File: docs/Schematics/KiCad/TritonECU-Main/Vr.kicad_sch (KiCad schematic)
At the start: 56 parts, among them J301 VR spare, U301 MAX9926UAEE+T, U302 MAX9926UAEE+T, U303 MAX9926UAEE+T

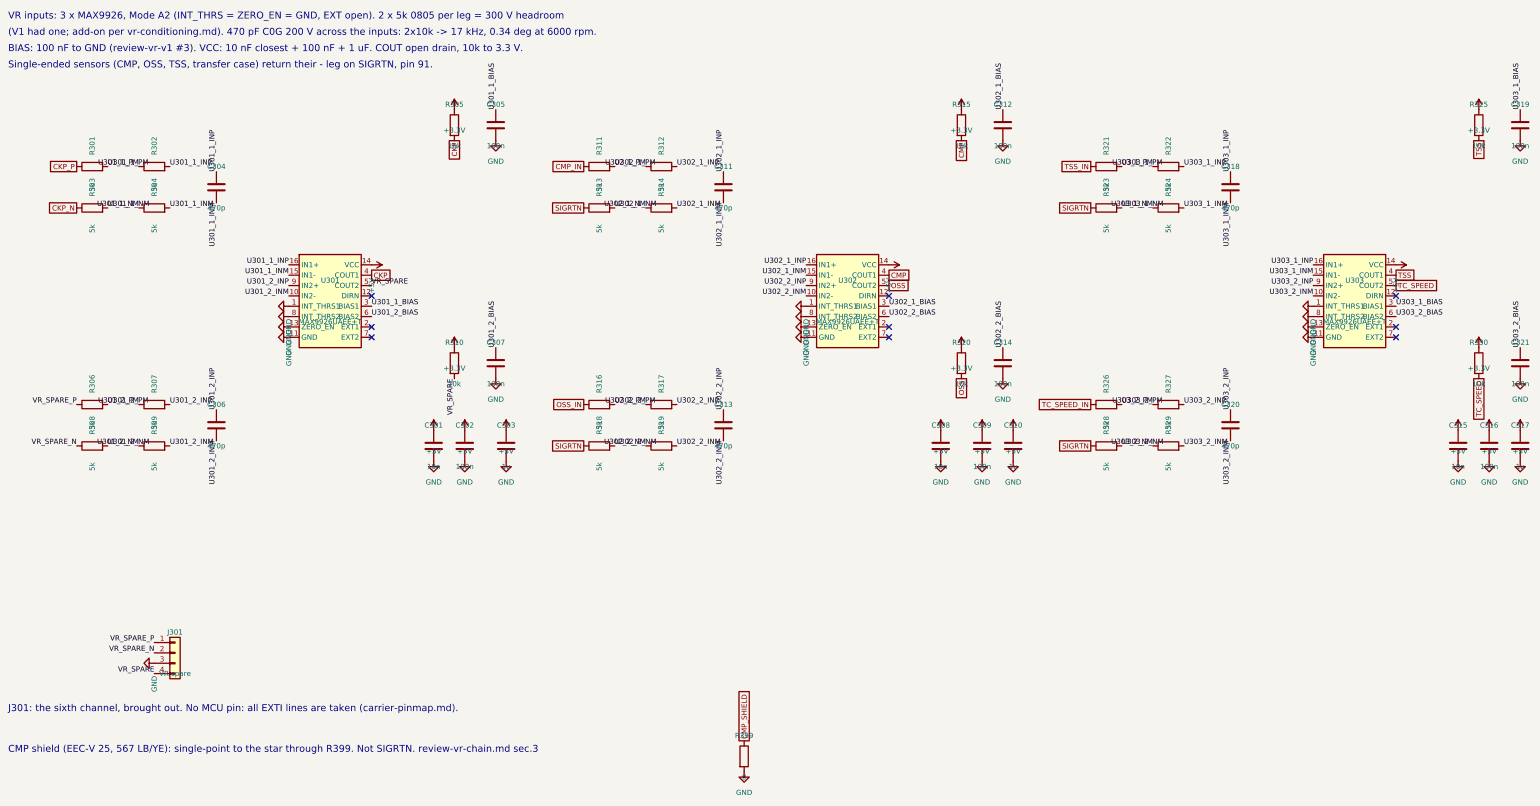
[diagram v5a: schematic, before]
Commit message: Carrier: Inputs sheet and switched rails for sleep
Inputs: one network per switch input - 4.7k pull-up to VPWR (ground-
switched only; VPWR so a TR bit closed in Park draws nothing parked),
SMF24A, 33k/15k, 10n, BAT54J to 3.3 V. TR1/2/4 and 4X4L ground-switched,
TR3A/BRAKE/ACP/TCS 12 V high-side. 4X4L mapped to EEC-V pin 14
(findings sec.14). IGN_WAKE from VPWR into PC13/WKUP4. TACH/SPEED bench
header, BOOT0 DFU solder jumper.

Switched rails: +5V and +3.3V stay up parked, so two TPS22917 load
switches on SW_RAIL_EN (PG12, 100k down) make +5V_SW / +3.3V_SW for the
running-only loads: 74HCT541 x3 and OE pull-ups, MAX9926 x3 and COUT
pull-ups, ADS8588H, OPA2376 x2, O2 bias, knock block, 74HC4051, TPS2H160B
FAULT pull-up, TFT pull-up. MCU, watchdog, CAN, SCP RX, clamps stay on.

gen_carrier_pcb.py: packer steps around existing parts, fills several
rects in turn, parks overflow below earlier parked parts.

Co-Authored-By: Claude Opus 5.5 <noreply@anthropic.com>
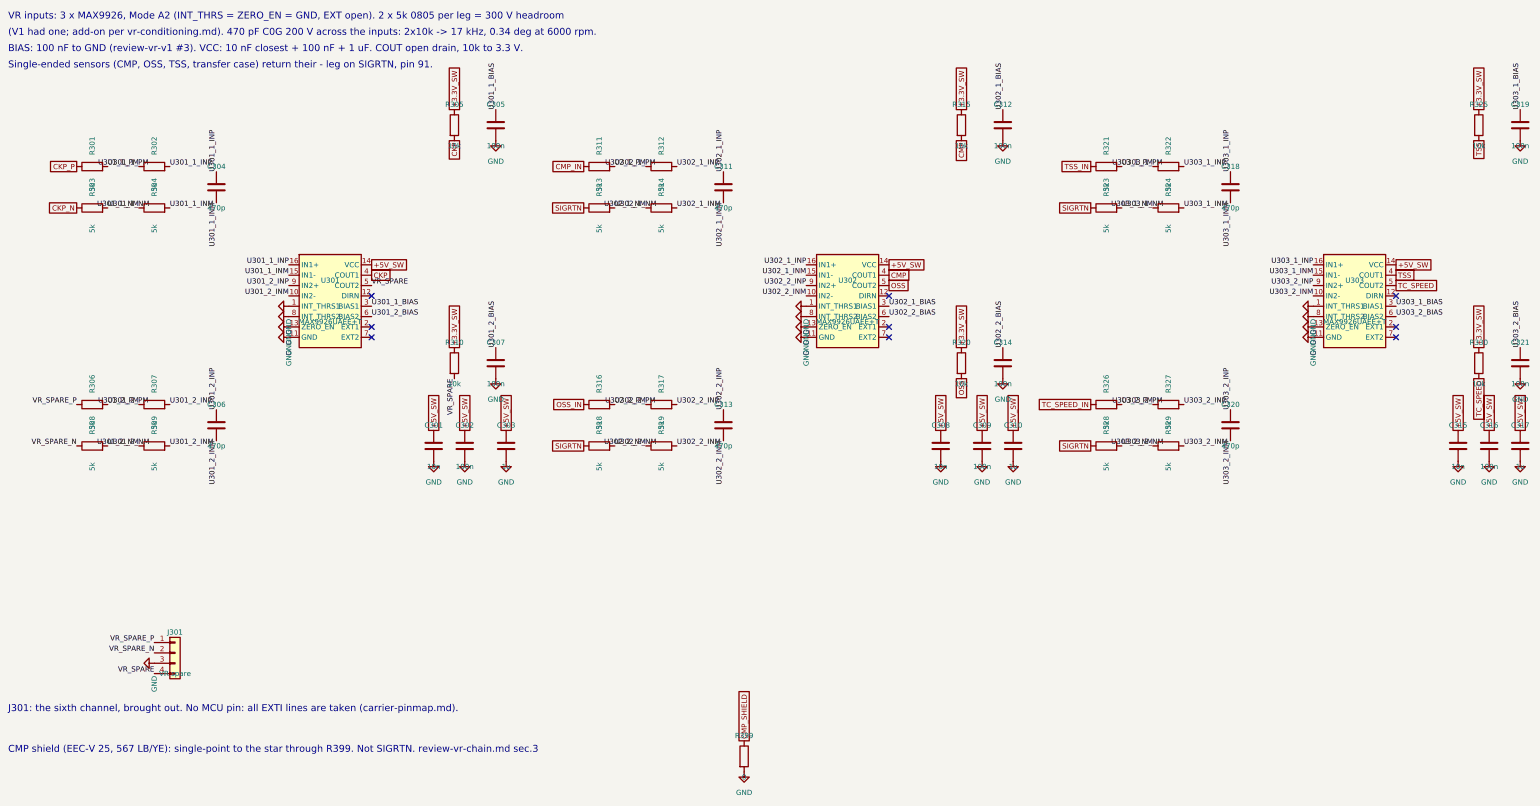
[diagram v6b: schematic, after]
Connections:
- net +3.3V renamed +3.3V_SW
- net +5V renamed +5V_SW
